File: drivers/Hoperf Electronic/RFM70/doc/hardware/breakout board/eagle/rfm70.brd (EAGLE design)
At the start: 20.3 x 17.8 mm, 4 parts, among them CON1 MICROHAL_CONNECTOR_M_1_REDUCE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

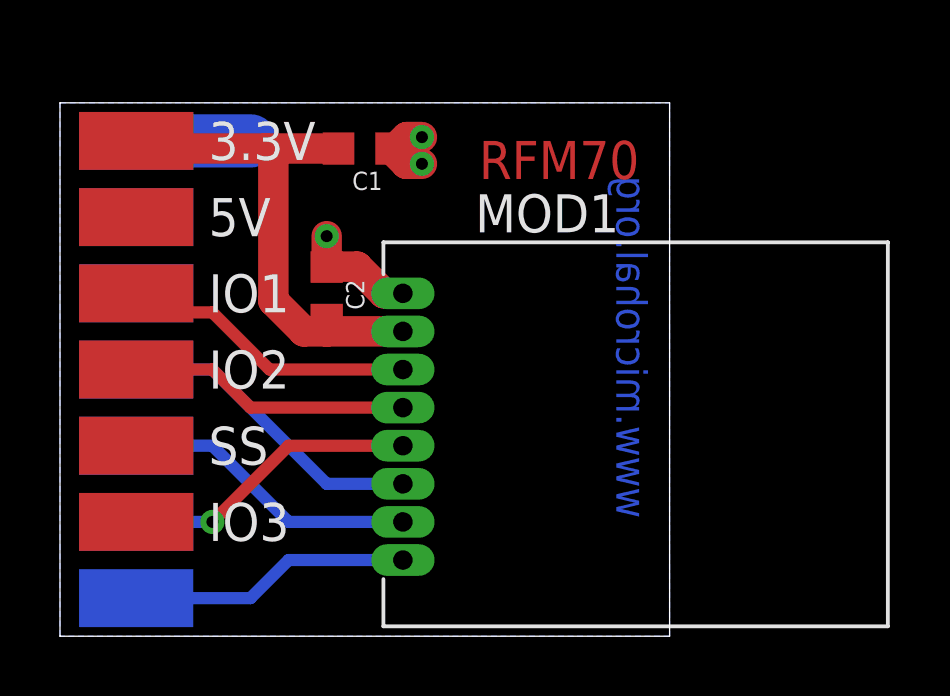
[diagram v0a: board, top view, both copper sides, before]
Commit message: RFM70 PCB - fixed bug on PCB.
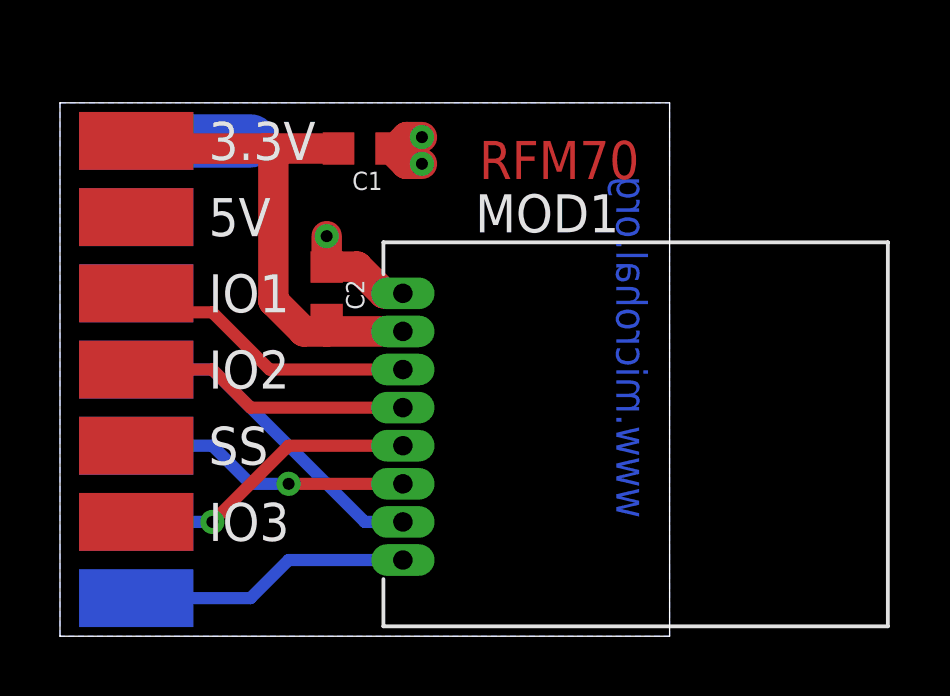
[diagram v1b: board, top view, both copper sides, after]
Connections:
- net MISO: now also CON1.7; no longer CON1.9
- net MOSI: now also CON1.9; no longer CON1.7
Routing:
- net MOSI: track 10.5 -> 9.42 mm, vias 0 -> 1
- net MISO: track 9.94 -> 11.0 mm
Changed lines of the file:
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@@
 <?xml version="1.0" encoding="utf-8"?>
 <!DOCTYPE eagle SYSTEM "eagle.dtd">
-<eagle version="7.3.0">
+<eagle version="7.5.0">
 <drawing>
 <settings>
@@
 </signal>
 <signal name="MOSI">
-<contactref element="CON1" pad="7"/>
 <contactref element="MOD1" pad="6"/>
-<wire x1="11.43" y1="5.08" x2="8.89" y2="5.08" width="0.4064" layer="16"/>
-<wire x1="8.89" y1="5.08" x2="5.08" y2="8.89" width="0.4064" layer="16"/>
-<wire x1="5.08" y1="8.89" x2="2.54" y2="8.89" width="0.4064" layer="16"/>
+<contactref element="CON1" pad="9"/>
+<wire x1="6.35" y1="5.08" x2="5.08" y2="6.35" width="0.4064" layer="16"/>
+<wire x1="5.08" y1="6.35" x2="2.54" y2="6.35" width="0.4064" layer="16"/>
+<wire x1="11.43" y1="5.08" x2="7.62" y2="5.08" width="0.4064" layer="1"/>
+<via x="7.62" y="5.08" extent="1-16" drill="0.4"/>
+<wire x1="7.62" y1="5.08" x2="6.35" y2="5.08" width="0.4064" layer="16"/>
 </signal>
 <signal name="MISO">
-<contactref element="CON1" pad="9"/>
 <contactref element="MOD1" pad="7"/>
-<wire x1="11.43" y1="3.81" x2="7.62" y2="3.81" width="0.4064" layer="16"/>
-<wire x1="7.62" y1="3.81" x2="5.08" y2="6.35" width="0.4064" layer="16"/>
-<wire x1="5.08" y1="6.35" x2="2.54" y2="6.35" width="0.4064" layer="16"/>
+<contactref element="CON1" pad="7"/>
+<wire x1="2.54" y1="8.89" x2="5.08" y2="8.89" width="0.4064" layer="16"/>
+<wire x1="5.08" y1="8.89" x2="10.16" y2="3.81" width="0.4064" layer="16"/>
+<wire x1="11.43" y1="3.81" x2="10.16" y2="3.81" width="0.4064" layer="16"/>
 </signal>
 <signal name="SCK">
